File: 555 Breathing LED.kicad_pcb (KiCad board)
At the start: 2 copper layers, 7 parts, among them Q1 Q_NPN_BCE, U1 LMC555xN

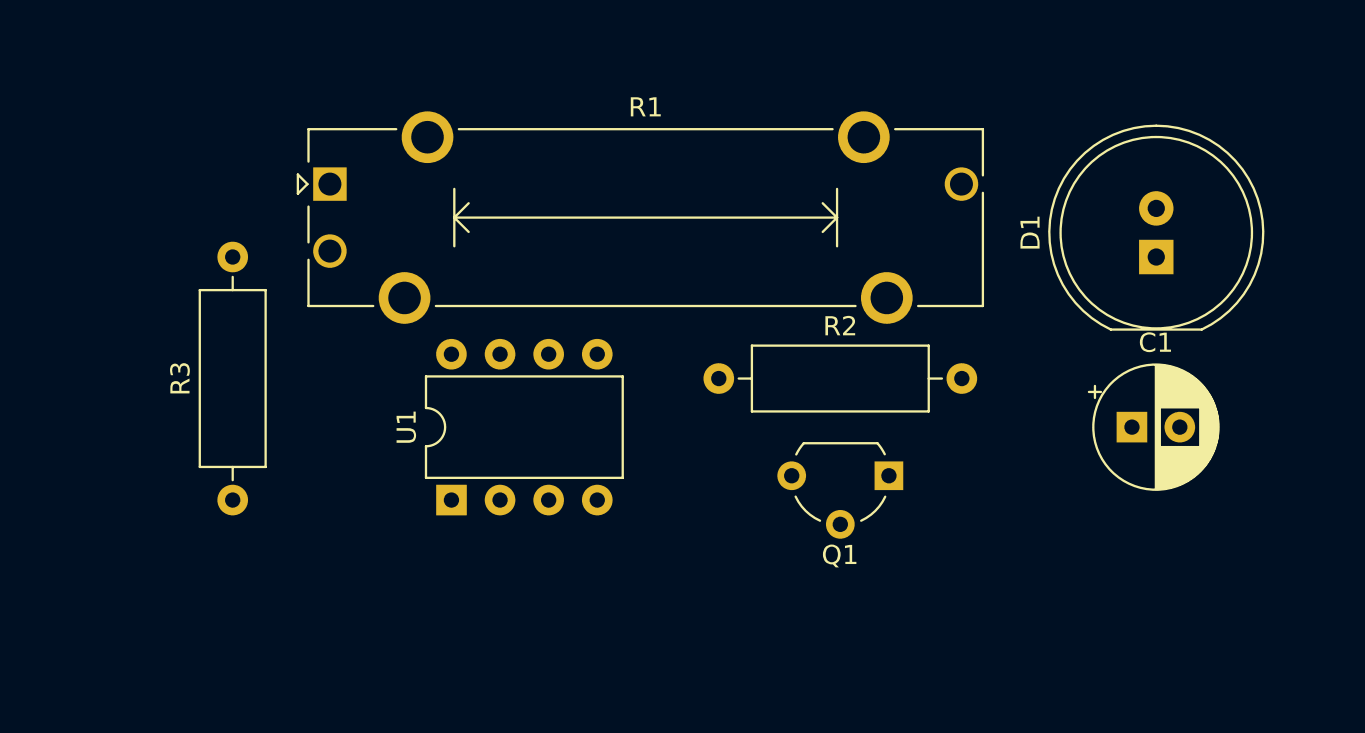
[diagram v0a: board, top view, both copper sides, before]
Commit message: Smaller Radius + m3 holes
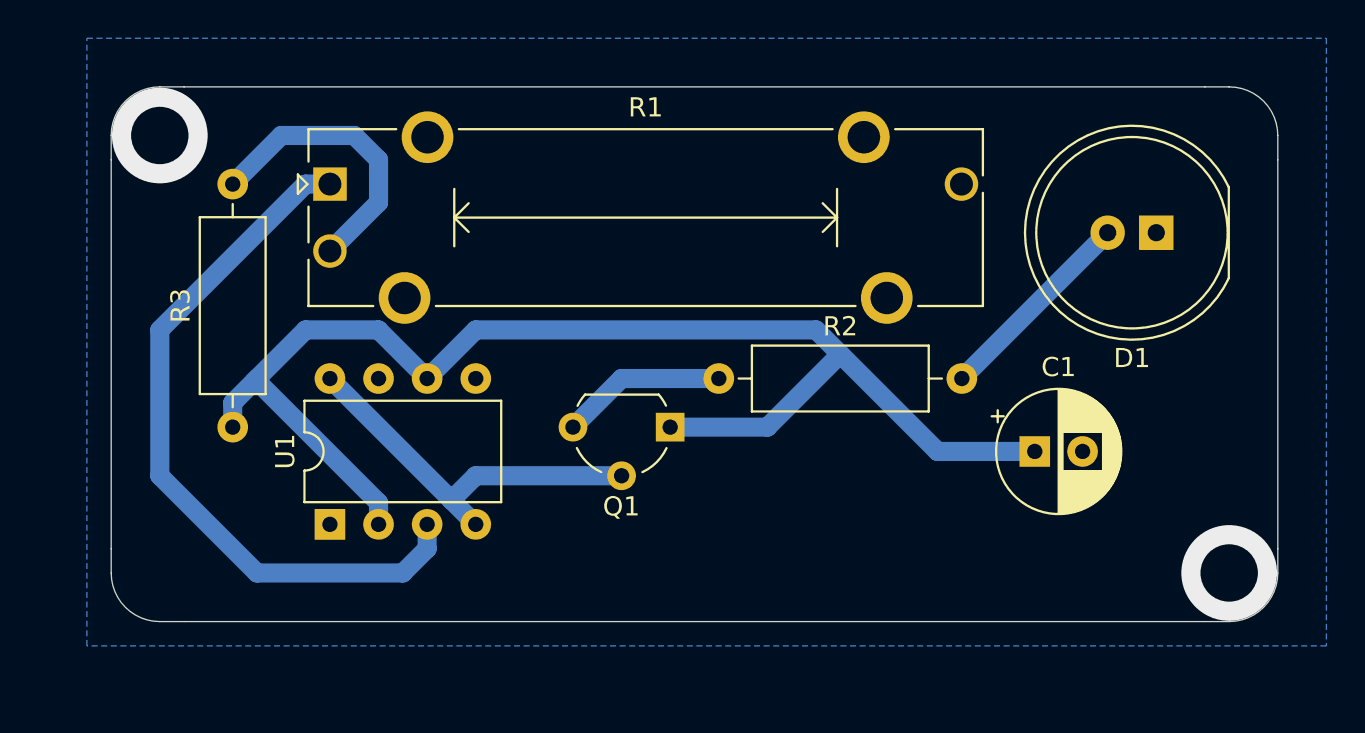
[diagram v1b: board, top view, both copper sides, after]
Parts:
- moved Q1 11.7 mm to (91.4, 82.5)
- moved U1 6.48 mm to (73.7, 87.6)
- moved C1 5.24 mm to (110.5, 83.8)
- moved R3 3.81 mm to (68.6, 82.5)
- moved D1 1.27 mm to (116.8, 72.4), turned to 180 degrees
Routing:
- net Net-(C1-Pad1): track 0.00 -> 70.2 mm
- net Net-(R1-Pad1): track 0.00 -> 37.5 mm
- net +5V: track 0.00 -> 20.2 mm
- net Net-(R1-Pad2): track 0.00 -> 15.0 mm
- net Net-(D1-Pad2): track 0.00 -> 10.8 mm
- net Net-(Q1-Pad3): track 0.00 -> 8.67 mm
- net GND: vias 0 -> 2
- added copper zone on B.Cu, net GND
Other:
- board outline added: 61 x 27.9 mm

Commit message: Fixed corners and m3 holes
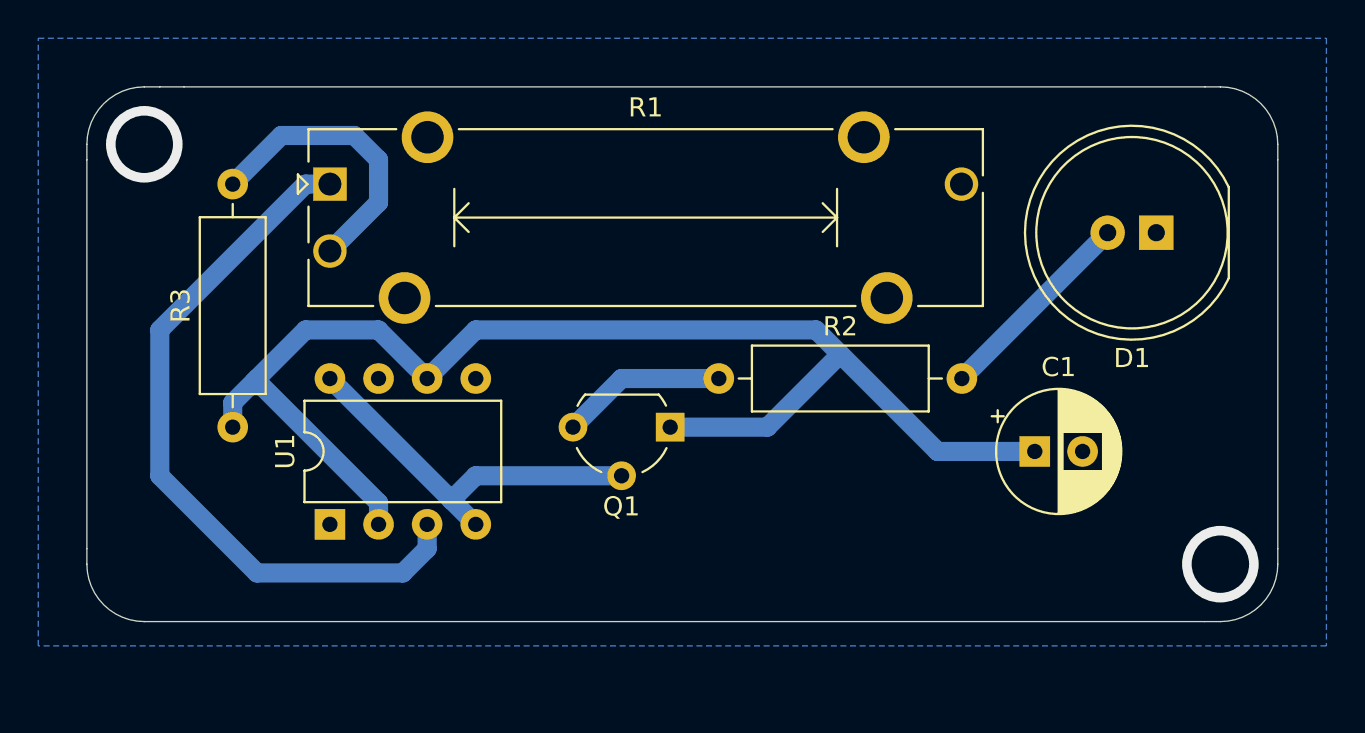
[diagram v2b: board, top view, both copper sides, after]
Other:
- board size 61 x 27.9 mm -> 62.2 x 27.9 mm
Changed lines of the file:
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@@
   (general
     (thickness 1.6)
-    (drawings 16)
+    (drawings 17)
     (tracks 37)
     (zones 0)
@@
     )
   )
-  (gr_line (start 120.65 64.77) (end 119.38 64.77) (layer Edge.Cuts) (width 0.05))
-  (gr_line (start 123.19 68.58) (end 123.19 67.31) (layer Edge.Cuts) (width 0.05))
-  (gr_line (start 123.19 88.9) (end 123.19 90.17) (layer Edge.Cuts) (width 0.05))
-  (gr_line (start 119.38 92.71) (end 120.65 92.71) (layer Edge.Cuts) (width 0.05))
+  (gr_line (start 60.96 89.71) (end 60.96 88.9) (layer Edge.Cuts) (width 0.05))
+  (gr_line (start 66.04 92.71) (end 63.96 92.71) (layer Edge.Cuts) (width 0.05))
+  (gr_arc (start 63.96 89.71) (end 60.96 89.71) (angle -90) (layer Edge.Cuts) (width 0.05))
+  (gr_line (start 120.19 64.77) (end 119.38 64.77) (layer Edge.Cuts) (width 0.05))
+  (gr_line (start 123.19 68.58) (end 123.19 67.77) (layer Edge.Cuts) (width 0.05))
+  (gr_arc (start 120.19 67.77) (end 123.19 67.77) (angle -90) (layer Edge.Cuts) (width 0.05))
+  (gr_line (start 60.96 67.77) (end 60.96 68.58) (layer Edge.Cuts) (width 0.05))
+  (gr_line (start 64.77 64.77) (end 63.96 64.77) (layer Edge.Cuts) (width 0.05))
+  (gr_arc (start 63.96 67.77) (end 63.96 64.77) (angle -90) (layer Edge.Cuts) (width 0.05))
+  (gr_line (start 123.19 89.71) (end 123.19 88.9) (layer Edge.Cuts) (width 0.05))
+  (gr_line (start 119.38 92.71) (end 120.19 92.71) (layer Edge.Cuts) (width 0.05))
+  (gr_arc (start 120.19 89.71) (end 120.19 92.71) (angle -90) (layer Edge.Cuts) (width 0.05))
   (gr_line (start 64.77 64.77) (end 66.04 64.77) (layer Edge.Cuts) (width 0.05))
-  (gr_line (start 62.23 68.58) (end 62.23 67.31) (layer Edge.Cuts) (width 0.05))
-  (gr_line (start 64.77 92.71) (end 66.04 92.71) (layer Edge.Cuts) (width 0.05))
-  (gr_line (start 62.23 88.9) (end 62.23 90.17) (layer Edge.Cuts) (width 0.05))
-  (gr_arc (start 64.77 90.17) (end 62.23 90.17) (angle -90) (layer Edge.Cuts) (width 0.05))
-  (gr_arc (start 64.77 67.31) (end 64.77 64.77) (angle -90) (layer Edge.Cuts) (width 0.05))
-  (gr_arc (start 120.65 67.31) (end 123.19 67.31) (angle -90) (layer Edge.Cuts) (width 0.05))
-  (gr_arc (start 120.65 90.17) (end 120.65 92.71) (angle -90) (layer Edge.Cuts) (width 0.05))
-  (gr_line (start 62.23 88.9) (end 62.23 68.58) (layer Edge.Cuts) (width 0.05))
+  (gr_line (start 60.96 88.9) (end 60.96 68.58) (layer Edge.Cuts) (width 0.05))
   (gr_line (start 119.38 92.71) (end 66.04 92.71) (layer Edge.Cuts) (width 0.05))
   (gr_line (start 123.19 68.58) (end 123.19 88.9) (layer Edge.Cuts) (width 0.05))
   (gr_line (start 66.04 64.77) (end 119.38 64.77) (layer Edge.Cuts) (width 0.05))
-  (via (at 120.65 90.17) (size 5) (drill 3) (layers F.Cu B.Cu) (net 1))
-  (via (at 64.77 67.31) (size 5) (drill 3) (layers F.Cu B.Cu) (net 1))
+  (via (at 120.19 89.71) (size 4) (drill 3) (layers F.Cu B.Cu) (net 1))
+  (via (at 63.96 67.77) (size 4) (drill 3) (layers F.Cu B.Cu) (net 1))
   (segment (start 76.2 86.49863) (end 69.85 80.14863) (width 1) (layer B.Cu) (net 2))
   (segment (start 76.2 87.63) (end 76.2 86.49863) (width 1) (layer B.Cu) (net 2))
@@
     (polygon
       (pts
-        (xy 125.73 93.98) (xy 60.96 93.98) (xy 60.96 62.23) (xy 125.73 62.23)
+        (xy 125.73 93.98) (xy 58.42 93.98) (xy 58.42 62.23) (xy 125.73 62.23)
       )
     )

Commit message: Updated Pcb and added graphics
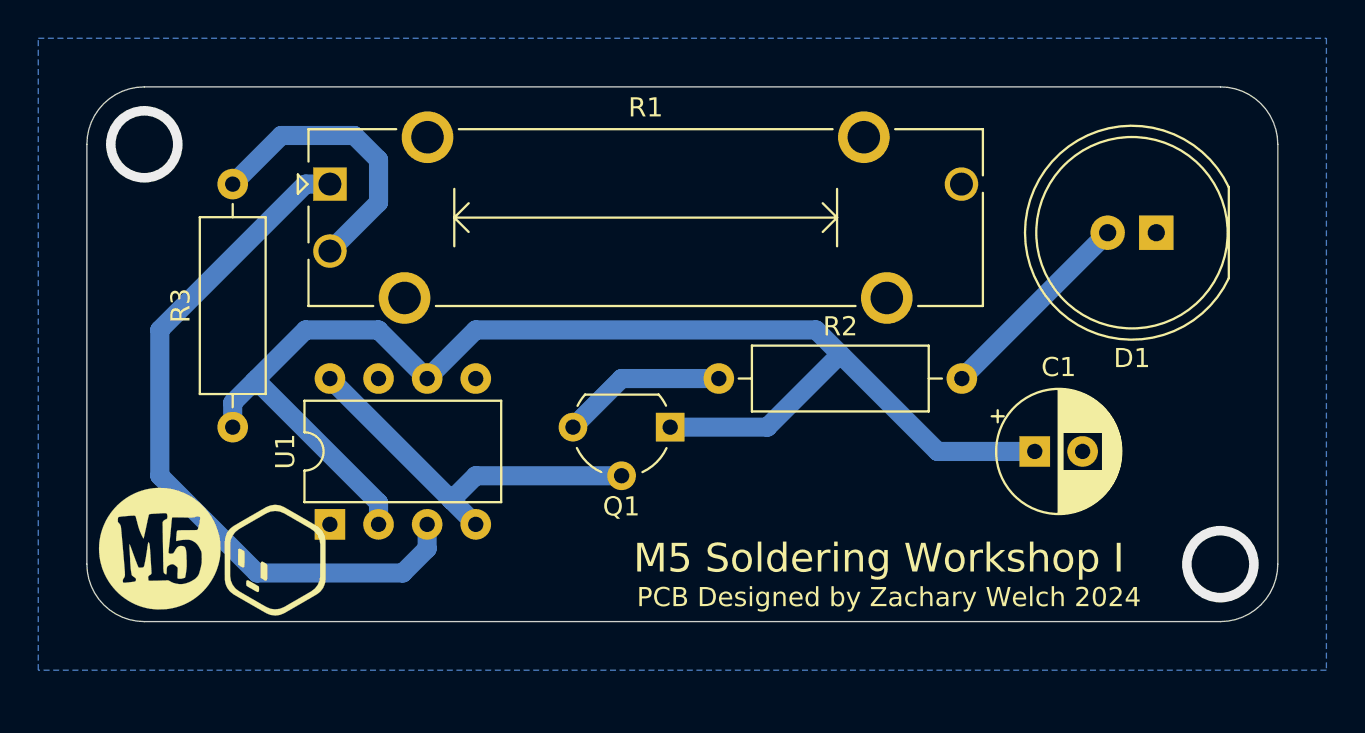
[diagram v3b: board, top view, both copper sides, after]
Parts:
- added ?: , 555-Breathing-LED:Smule Logo, F.Cu at (70.8, 89.5)
- added ?: , 555-Breathing-LED:M5 Logo, F.Cu at (64.8, 88.9)
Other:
- outline, holes or cut-outs redrawn
- board text added: "M5 Soldering Workshop I"
- board text added: "PCB Designed by Zachary Welch 2024"

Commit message: Updated PCB + Schematic
Added battery holder
Made PCB wider
Moved ground plane to top layer
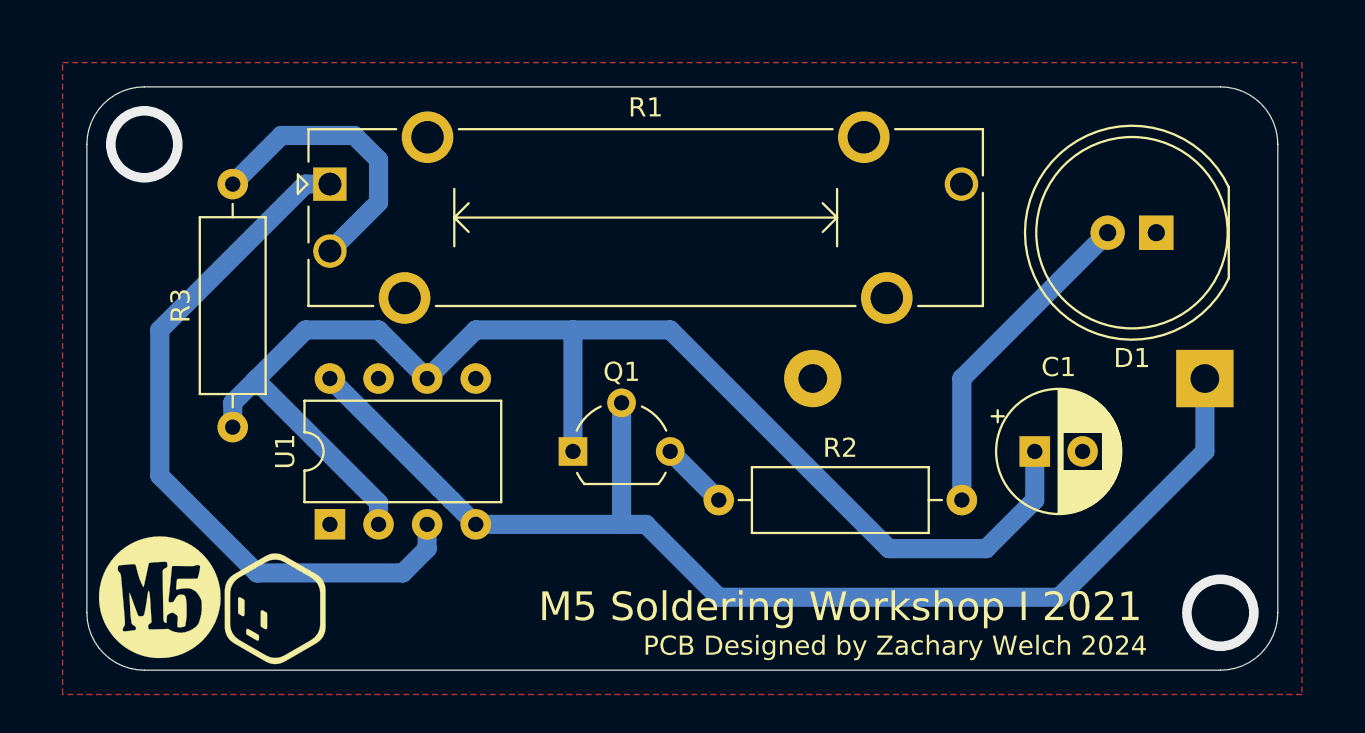
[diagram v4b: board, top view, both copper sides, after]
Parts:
- added BT1: Battery_Cell, Battery:BatteryHolder_Keystone_107_1x23mm, B.Cu at (119.4, 80.0)
- moved R2 6.35 mm to (94.0, 86.4)
- moved Q1 5.24 mm to (86.4, 83.8), turned to 0 degrees
- moved ? 2.54 mm to (70.8, 92.0)
- moved ? 2.54 mm to (64.8, 91.4)
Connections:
- net +5V renamed VCC
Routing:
- net VCC: track 20.2 -> 63.8 mm
- net Net-(D1-Pad2): track 10.8 -> 17.1 mm
- net Net-(Q1-Pad3): track 8.67 -> 3.59 mm
- net Net-(C1-Pad1): track 70.2 -> 71.7 mm
- added copper zone on F.Cu, net GND
- removed copper zone on B.Cu, net GND
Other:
- board size 62.2 x 27.9 mm -> 62.2 x 30.5 mm
- board text added: "Fall 2021"
- board text added: "M5 Soldering Workshop I 2021"
- board text added: "Saturday is for the makers!"
- board text removed: "M5 Soldering Workshop I"

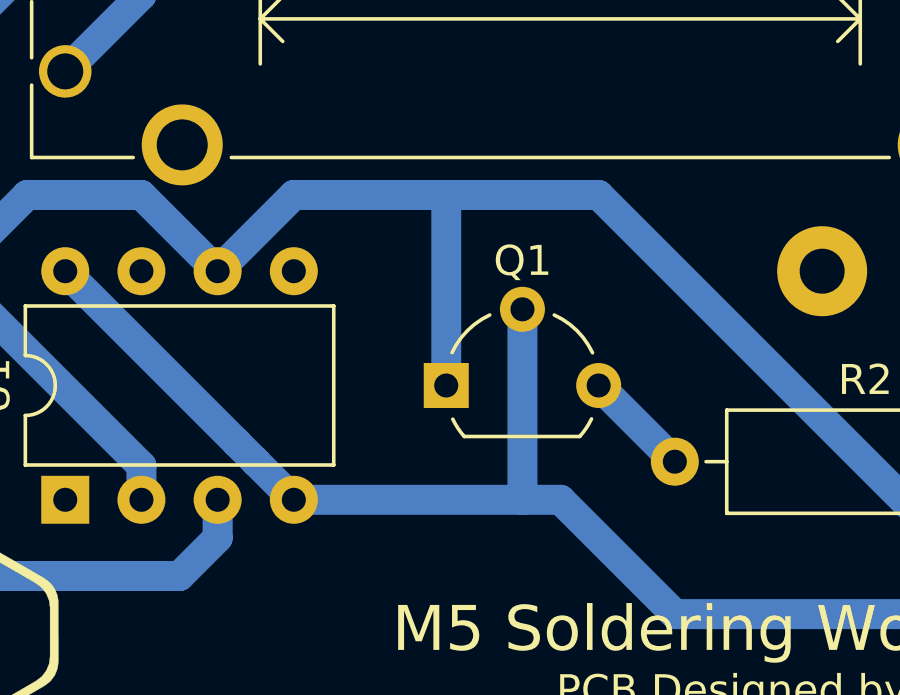
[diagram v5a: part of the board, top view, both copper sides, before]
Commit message: Fixed BJT
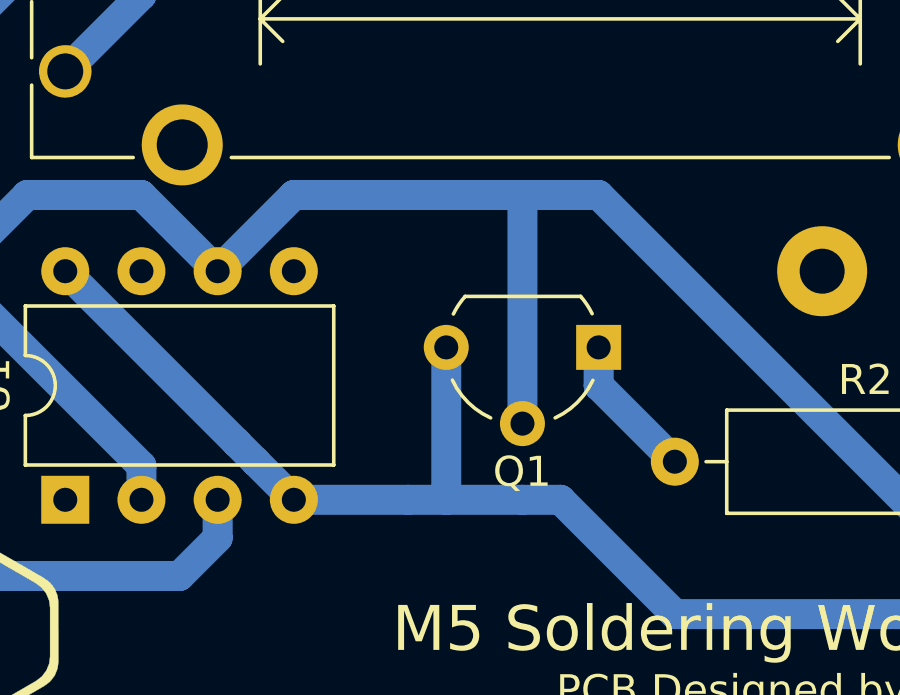
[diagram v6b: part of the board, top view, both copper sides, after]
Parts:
- Q1: value Q_NPN_BCE -> Q_NPN_EBC
- moved Q1 5.24 mm to (91.4, 82.5), turned to 180 degrees
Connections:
- Q1 pad 1: Net-(C1-Pad1) -> Net-(Q1-Pad1)
- Q1 pad 2: VCC -> Net-(C1-Pad1)
- Q1 pad 3: Net-(Q1-Pad3) -> VCC
- R2 pad 1: Net-(Q1-Pad3) -> Net-(Q1-Pad1)
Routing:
- net Net-(Q1-Pad1): track 0.00 -> 4.86 mm
- net Net-(Q1-Pad3): track 3.59 -> 0.00 mm
- net Net-(C1-Pad1): track 71.7 -> 73.0 mm
- net VCC: track 63.8 -> 62.5 mm
